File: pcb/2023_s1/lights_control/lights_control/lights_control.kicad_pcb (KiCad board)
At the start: 2 copper layers, 16 parts, among them Q1 TIP122, U1 4N25, U2 40106

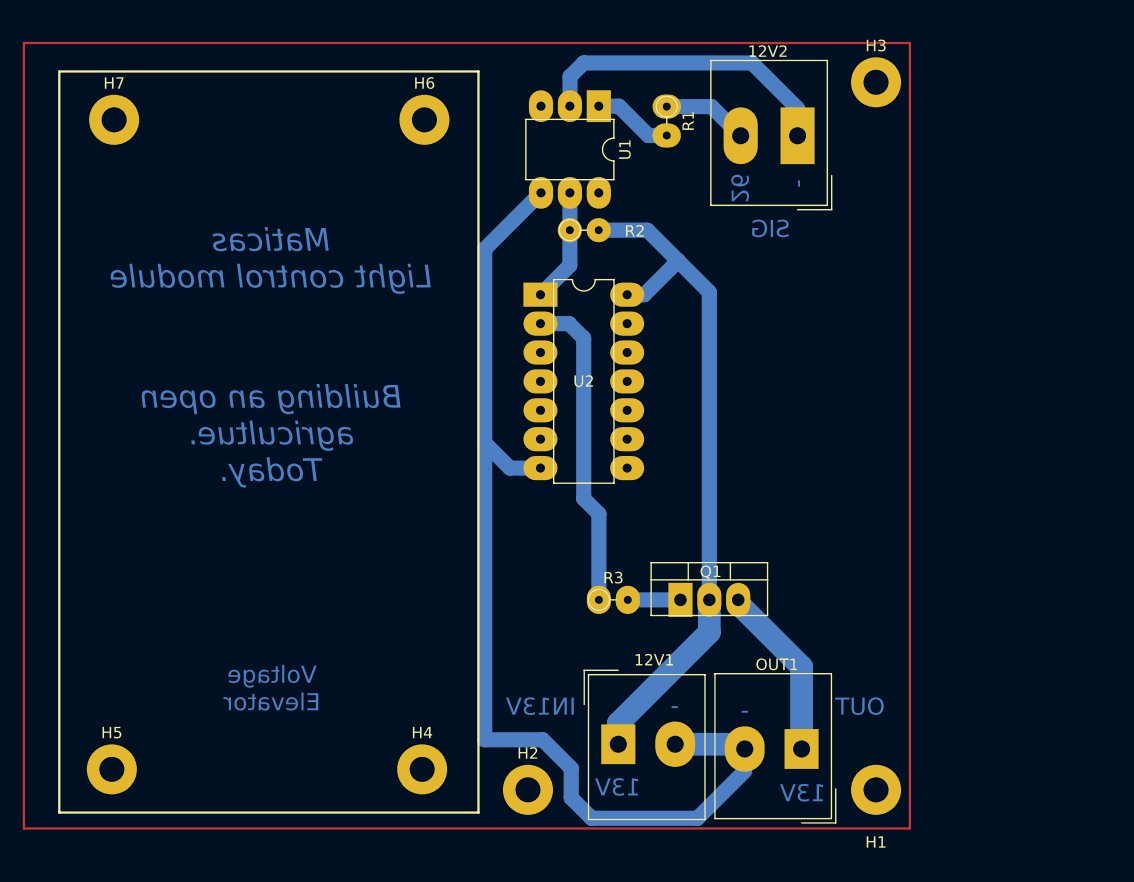
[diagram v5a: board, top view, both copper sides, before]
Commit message: update, changed pcbs to use mechanic relays instead of the trigger schmith circuit, because of reliability and simpleness of the design
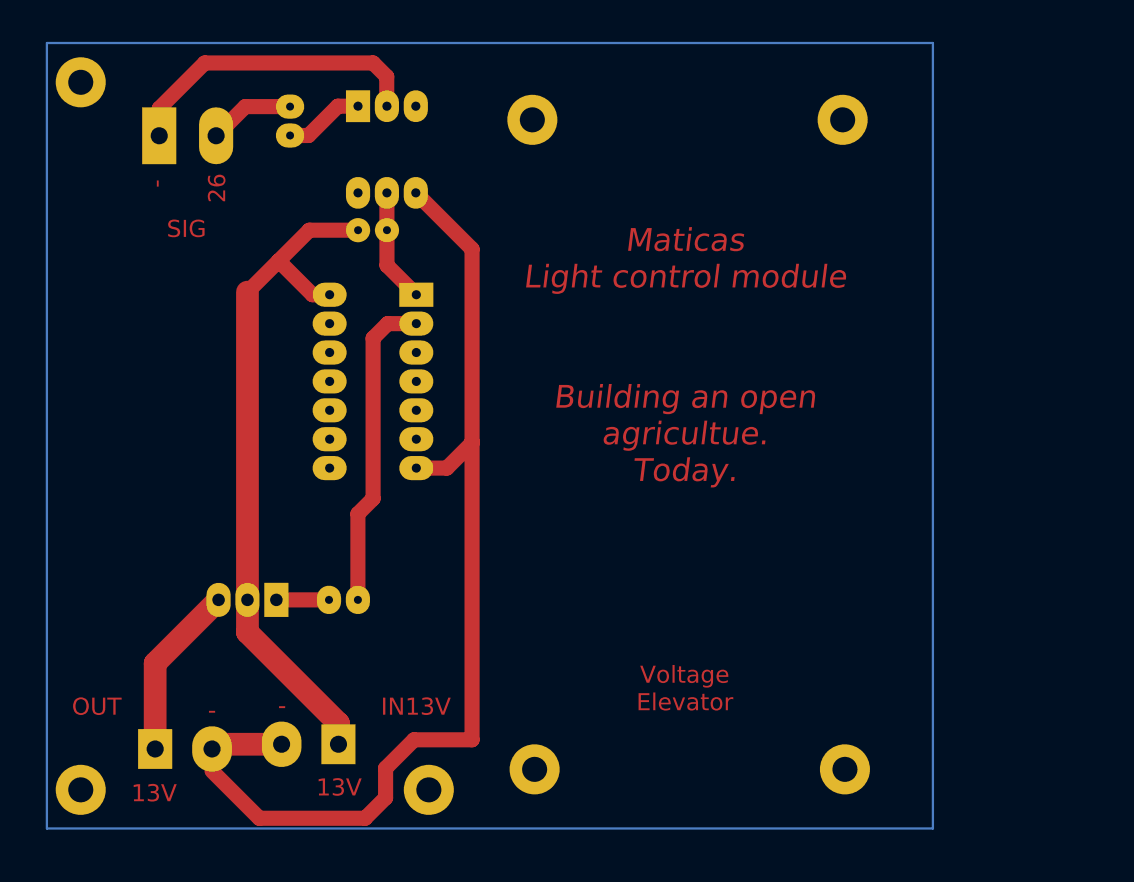
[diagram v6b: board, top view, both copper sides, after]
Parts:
- 12V1, 12V2, H1, H2, H3, H4, H5, H6, H7, OUT1, Q1, R1, R2, R3, U1, U2: moved to B.Cu
- moved H1 69.9 mm to (61.3, 118.0), turned to 180 degrees
- moved H3 69.9 mm to (61.3, 55.8), turned to 180 degrees
- moved H5 64.4 mm to (128.5, 116.2), turned to 180 degrees
- moved H7 64.0 mm to (128.3, 59.1), turned to 180 degrees
- moved OUT1 56.8 mm to (67.8, 114.4), turned to 0 degrees
- moved 12V2 56.1 mm to (68.2, 60.5), turned to 0 degrees
- moved Q1 35.5 mm to (78.5, 101.3), turned to 180 degrees
- moved R1 33.1 mm to (79.7, 57.9)
- moved 12V1 24.6 mm to (83.9, 114.0), turned to 180 degrees
- moved R3 21.2 mm to (85.6, 101.3), turned to 180 degrees
- moved U1 21.2 mm to (85.7, 57.9)
- moved R2 16.1 mm to (88.2, 68.8), turned to 180 degrees
- moved U2 10.9 mm to (90.8, 74.5), turned to 180 degrees
- moved H4 9.89 mm to (101.2, 116.2), turned to 180 degrees
- moved H6 9.49 mm to (101.0, 59.1), turned to 180 degrees
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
